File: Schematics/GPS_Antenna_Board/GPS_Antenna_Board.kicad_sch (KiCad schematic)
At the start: 22 parts, among them J1 470804001, U3 SAM-M10Q, U8 LM66100DCKR

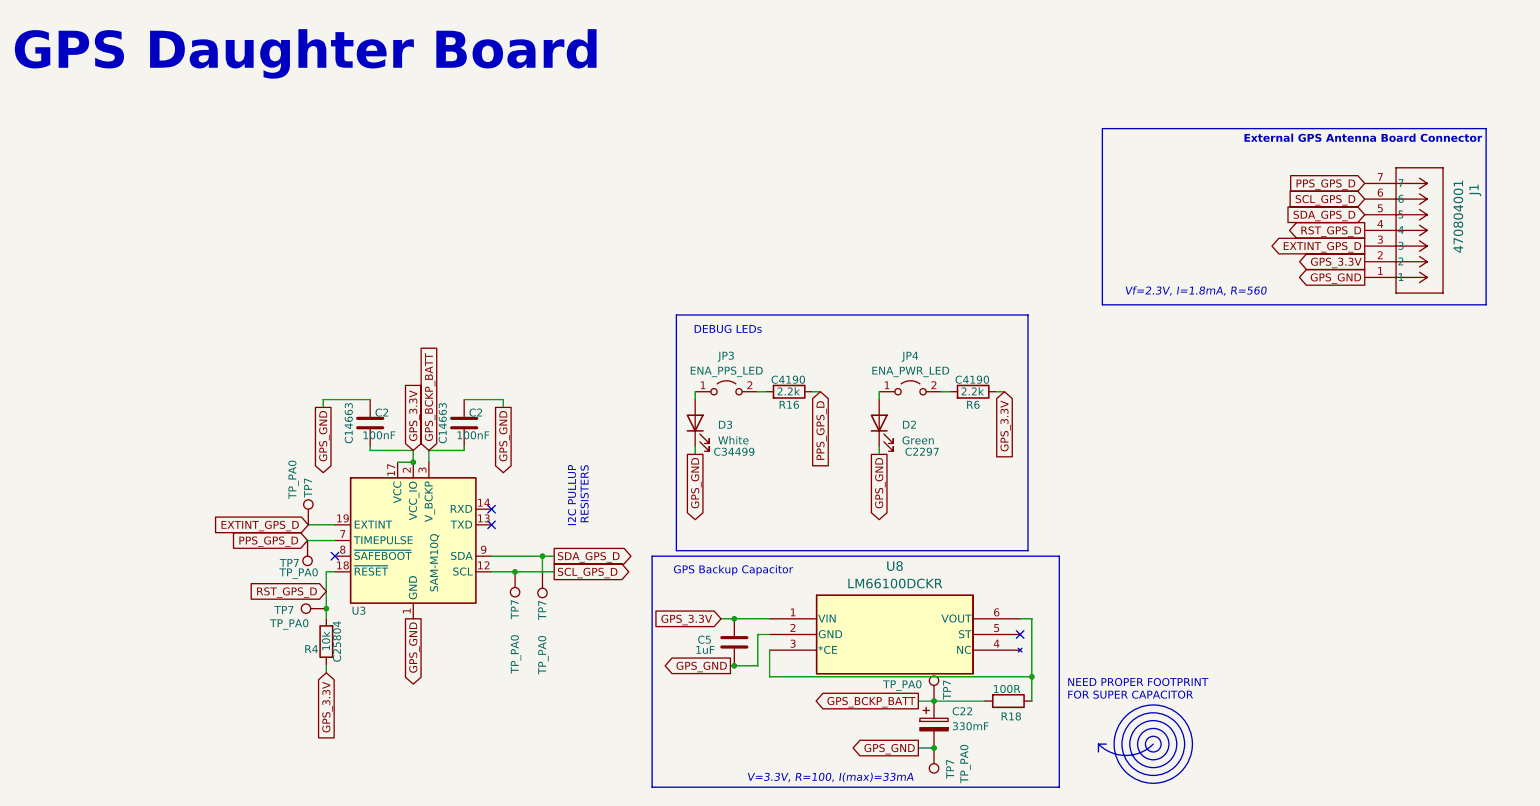
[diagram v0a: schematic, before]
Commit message: Cleaned up GPS antenna schematic
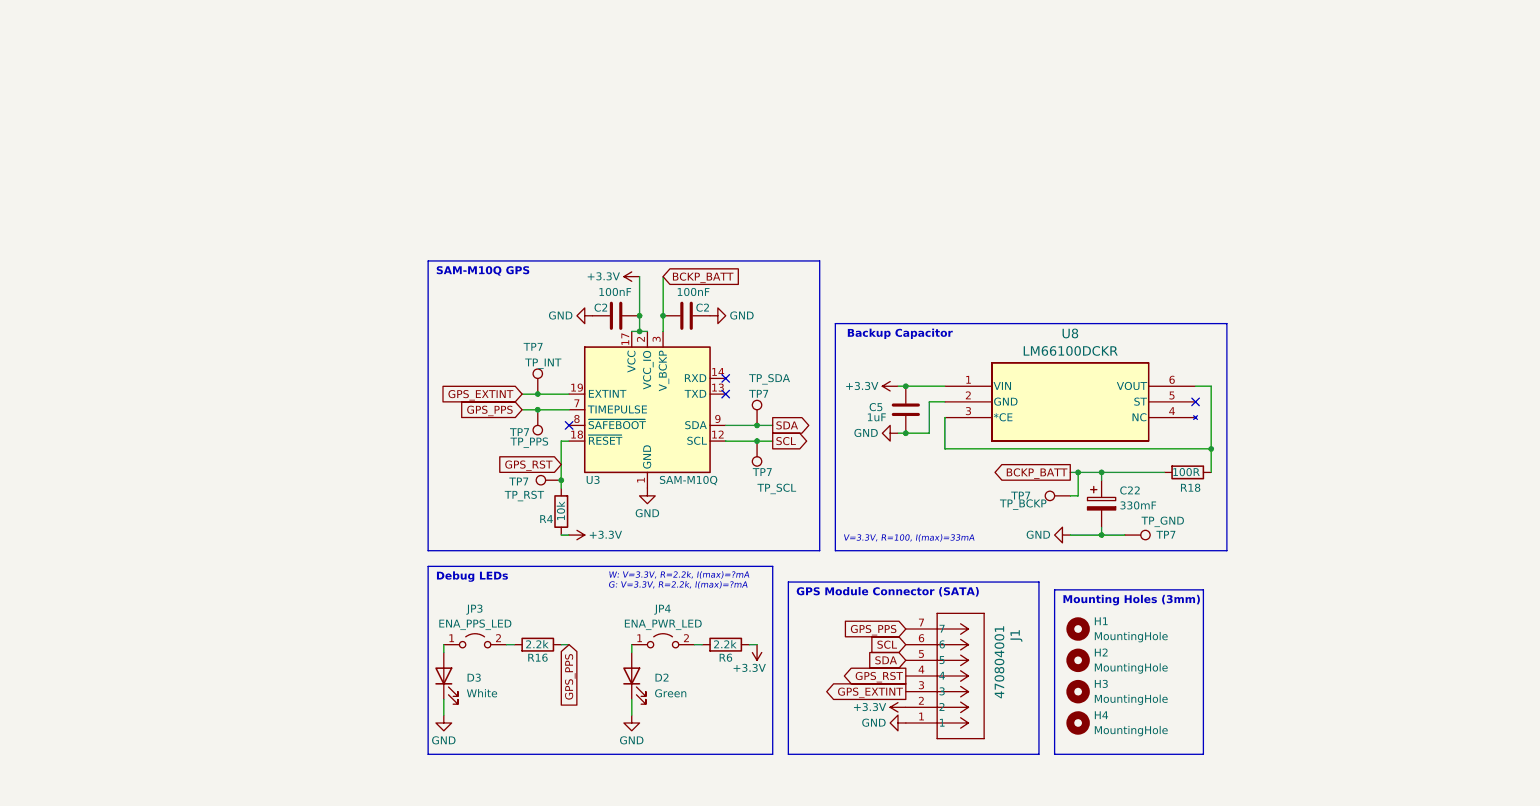
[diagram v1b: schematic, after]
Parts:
- added H1, H2, H3, H4: MountingHole, MountingHole:MountingHole_3mm_Pad, symbol Mechanical:MountingHole
- JP3, JP4: now left out of the parts list
- TP7: value TP_PA0 -> TP_GND; now left out of the parts list
- TP7: value TP_PA0 -> TP_PPS; now left out of the parts list
- TP7: value TP_PA0 -> TP_SDA; now left out of the parts list
- TP7: value TP_PA0 -> TP_BCKP; now left out of the parts list
- TP7: value TP_PA0 -> TP_RST; now left out of the parts list
- TP7: value TP_PA0 -> TP_INT; now left out of the parts list
- TP7: value TP_PA0 -> TP_SCL; now left out of the parts list
- U8: Digikey 296-53541-1-ND -> (none); LCSC (none) -> C2869734
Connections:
- net EXTINT_GPS_D renamed GPS_EXTINT
- net GPS_3.3V renamed +3.3V
- net GPS_BCKP_BATT renamed BCKP_BATT
- net BCKP_BATT: now also C2.1; no longer C2.2
- net GPS_GND renamed GND
- net GND: now also C2.2; no longer C2.1
- net PPS_GPS_D renamed GPS_PPS
- net RST_GPS_D renamed GPS_RST
- net SCL_GPS_D renamed SCL
- net SDA_GPS_D renamed SDA
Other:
- note added: "Backup Capacitor"
- note added: "Debug LEDs"
- note added: "GPS Module Connector (SATA)"
- note added: "Mounting Holes (3mm)"
- note added: "SAM-M10Q GPS"
- note added: "W: V=3.3V, R=2.2k, I(max)=?mA G: V=3.3V, R=2.2k, I(max)=?mA"
- note removed: "DEBUG LEDs"
- note removed: "External GPS Antenna Board Connector"
- note removed: "GPS Backup Capacitor"
- note removed: "GPS Daughter Board"
- note removed: "I2C PULLUP RESISTERS"
- note removed: "NEED PROPER FOOTPRINT FOR SUPER CAPACITOR"
- note removed: "Vf=2.3V, I=1.8mA, R=560"
- company: (none) -> Queen's Rocket Engineering Team
- title: (none) -> QRET 23-24 SRAD GPS Antenna Board
- moved on the sheet: C2, C22, C5, D2, D3, J1, JP3, JP4, R16, R18, R4, R6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

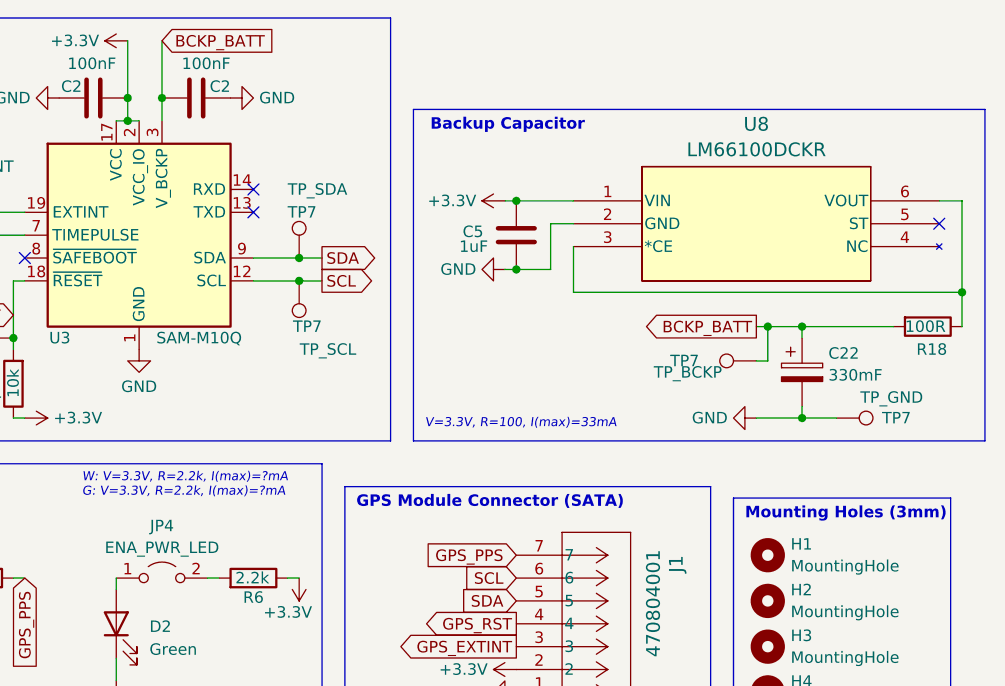
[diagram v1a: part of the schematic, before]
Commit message: Added mounting holes to GPS antenna board
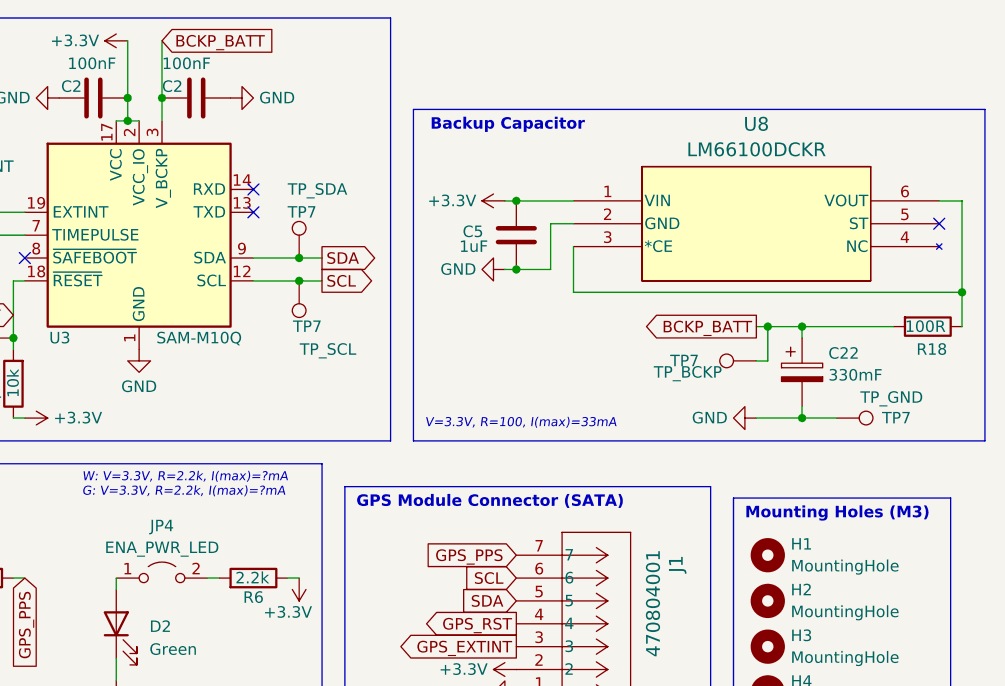
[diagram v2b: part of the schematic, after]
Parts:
- H1, H2, H3, H4: footprint MountingHole:MountingHole_3mm_Pad -> MountingHole:MountingHole_3.2mm_M3_DIN965_Pad
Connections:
- net BCKP_BATT: now also C2.2; no longer C2.1
- net GND: now also C2.1; no longer C2.2
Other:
- note added: "Mounting Holes (M3)"
- note removed: "Mounting Holes (3mm)"
- moved on the sheet: C2
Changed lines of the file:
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@@
     (comment 4 "GRID = 1.27mm")
   )
+  (junction (at 119.38 62.23) (diameter 0) (color 0 0 0 0)
+  )
   (junction (at 99.06 77.47) (diameter 0) (color 0 0 0 0)
   )
@@
   )
   (junction (at 186.69 87.63) (diameter 0) (color 0 0 0 0)
-  )
-  (junction (at 119.38 62.23) (diameter 0) (color 0 0 0 0)
   )
   (junction (at 134.62 80.01) (diameter 0) (color 0 0 0 0)
@@
     (stroke (width 0) (type default))
   )
+  (wire (pts (xy 119.38 55.88) (xy 119.38 62.23))
+    (stroke (width 0) (type default))
+  )
+  (wire (pts (xy 114.3 124.46) (xy 114.3 127))
+    (stroke (width 0) (type default))
+  )
+  (wire (pts (xy 158.75 73.66) (xy 165.1 73.66))
+    (stroke (width 0) (type default))
+  )
+  (wire (pts (xy 162.56 81.28) (xy 162.56 76.2))
+    (stroke (width 0) (type default))
+  )
+  (wire (pts (xy 190.5 97.79) (xy 194.31 97.79))
+    (stroke (width 0) (type default))
+  )
+  (wire (pts (xy 185.42 87.63) (xy 186.69 87.63))
+    (stroke (width 0) (type default))
+  )
+  (wire (pts (xy 93.98 115.57) (xy 95.25 115.57))
+    (stroke (width 0) (type default))
+  )
+  (wire (pts (xy 124.46 115.57) (xy 125.73 115.57))
+    (stroke (width 0) (type default))
+  )
+  (wire (pts (xy 190.5 87.63) (xy 200.66 87.63))
+    (stroke (width 0) (type default))
+  )
+  (wire (pts (xy 186.69 91.44) (xy 186.69 87.63))
+    (stroke (width 0) (type default))
+  )
+  (wire (pts (xy 165.1 78.74) (xy 165.1 83.82))
+    (stroke (width 0) (type default))
+  )
+  (wire (pts (xy 114.3 64.77) (xy 115.57 64.77))
+    (stroke (width 0) (type default))
+  )
+  (wire (pts (xy 134.62 80.01) (xy 137.16 80.01))
+    (stroke (width 0) (type default))
+  )
+  (wire (pts (xy 83.82 115.57) (xy 83.82 116.84))
+    (stroke (width 0) (type default))
+  )
+  (wire (pts (xy 134.62 82.55) (xy 137.16 82.55))
+    (stroke (width 0) (type default))
+  )
+  (wire (pts (xy 102.87 90.17) (xy 102.87 88.9))
+    (stroke (width 0) (type default))
+  )
+  (wire (pts (xy 96.52 77.47) (xy 99.06 77.47))
+    (stroke (width 0) (type default))
+  )
+  (wire (pts (xy 157.48 81.28) (xy 158.75 81.28))
+    (stroke (width 0) (type default))
+  )
+  (wire (pts (xy 83.82 124.46) (xy 83.82 127))
+    (stroke (width 0) (type default))
+  )
+  (wire (pts (xy 114.3 115.57) (xy 114.3 116.84))
+    (stroke (width 0) (type default))
+  )
+  (wire (pts (xy 102.87 82.55) (xy 104.14 82.55))
+    (stroke (width 0) (type default))
+  )
+  (wire (pts (xy 99.06 77.47) (xy 104.14 77.47))
+    (stroke (width 0) (type default))
+  )
+  (wire (pts (xy 185.42 91.44) (xy 186.69 91.44))
+    (stroke (width 0) (type default))
+  )
+  (wire (pts (xy 157.48 73.66) (xy 158.75 73.66))
+    (stroke (width 0) (type default))
+  )
+  (wire (pts (xy 186.69 87.63) (xy 190.5 87.63))
+    (stroke (width 0) (type default))
+  )
+  (wire (pts (xy 129.54 82.55) (xy 134.62 82.55))
+    (stroke (width 0) (type default))
+  )
+  (wire (pts (xy 165.1 83.82) (xy 208.28 83.82))
+    (stroke (width 0) (type default))
+  )
+  (wire (pts (xy 208.28 83.82) (xy 208.28 73.66))
+    (stroke (width 0) (type default))
+  )
+  (wire (pts (xy 190.5 96.52) (xy 190.5 97.79))
+    (stroke (width 0) (type default))
+  )
+  (wire (pts (xy 208.28 73.66) (xy 205.74 73.66))
+    (stroke (width 0) (type default))
+  )
   (wire (pts (xy 119.38 62.23) (xy 119.38 64.77))
-    (stroke (width 0) (type default))
-  )
-  (wire (pts (xy 114.3 124.46) (xy 114.3 127))
-    (stroke (width 0) (type default))
-  )
-  (wire (pts (xy 158.75 73.66) (xy 165.1 73.66))
-    (stroke (width 0) (type default))
-  )
-  (wire (pts (xy 119.38 55.88) (xy 119.38 62.23))
-    (stroke (width 0) (type default))
-  )
-  (wire (pts (xy 162.56 81.28) (xy 162.56 76.2))
-    (stroke (width 0) (type default))
-  )
-  (wire (pts (xy 190.5 97.79) (xy 194.31 97.79))
-    (stroke (width 0) (type default))
-  )
-  (wire (pts (xy 185.42 87.63) (xy 186.69 87.63))
-    (stroke (width 0) (type default))
-  )
-  (wire (pts (xy 93.98 115.57) (xy 95.25 115.57))
-    (stroke (width 0) (type default))
-  )
-  (wire (pts (xy 124.46 115.57) (xy 125.73 115.57))
-    (stroke (width 0) (type default))
-  )
-  (wire (pts (xy 190.5 87.63) (xy 200.66 87.63))
-    (stroke (width 0) (type default))
-  )
-  (wire (pts (xy 186.69 91.44) (xy 186.69 87.63))
-    (stroke (width 0) (type default))
-  )
-  (wire (pts (xy 165.1 78.74) (xy 165.1 83.82))
-    (stroke (width 0) (type default))
-  )
-  (wire (pts (xy 114.3 64.77) (xy 115.57 64.77))
-    (stroke (width 0) (type default))
-  )
-  (wire (pts (xy 134.62 80.01) (xy 137.16 80.01))
-    (stroke (width 0) (type default))
-  )
-  (wire (pts (xy 83.82 115.57) (xy 83.82 116.84))
-    (stroke (width 0) (type default))
-  )
-  (wire (pts (xy 134.62 82.55) (xy 137.16 82.55))
-    (stroke (width 0) (type default))
-  )
-  (wire (pts (xy 102.87 90.17) (xy 102.87 88.9))
-    (stroke (width 0) (type default))
-  )
-  (wire (pts (xy 96.52 77.47) (xy 99.06 77.47))
-    (stroke (width 0) (type default))
-  )
-  (wire (pts (xy 157.48 81.28) (xy 158.75 81.28))
-    (stroke (width 0) (type default))
-  )
-  (wire (pts (xy 83.82 124.46) (xy 83.82 127))
-    (stroke (width 0) (type default))
-  )
-  (wire (pts (xy 114.3 115.57) (xy 114.3 116.84))
-    (stroke (width 0) (type default))
-  )
-  (wire (pts (xy 102.87 82.55) (xy 104.14 82.55))
-    (stroke (width 0) (type default))
-  )
-  (wire (pts (xy 99.06 77.47) (xy 104.14 77.47))
-    (stroke (width 0) (type default))
-  )
-  (wire (pts (xy 185.42 91.44) (xy 186.69 91.44))
-    (stroke (width 0) (type default))
-  )
-  (wire (pts (xy 157.48 73.66) (xy 158.75 73.66))
-    (stroke (width 0) (type default))
-  )
-  (wire (pts (xy 186.69 87.63) (xy 190.5 87.63))
-    (stroke (width 0) (type default))
-  )
-  (wire (pts (xy 129.54 82.55) (xy 134.62 82.55))
-    (stroke (width 0) (type default))
-  )
-  (wire (pts (xy 165.1 83.82) (xy 208.28 83.82))
-    (stroke (width 0) (type default))
-  )
-  (wire (pts (xy 208.28 83.82) (xy 208.28 73.66))
-    (stroke (width 0) (type default))
-  )
-  (wire (pts (xy 190.5 96.52) (xy 190.5 97.79))
-    (stroke (width 0) (type default))
-  )
-  (wire (pts (xy 208.28 73.66) (xy 205.74 73.66))
     (stroke (width 0) (type default))
   )
@@
     (effects (font (size 1 1) italic) (justify left bottom))
   )
-  (text "Mounting Holes (3mm)" (at 184.15 109.22 0)
+  (text "Mounting Holes (M3)" (at 184.15 109.22 0)
     (effects (font (size 1.27 1.27) (thickness 0.254) bold) (justify left bottom))
   )
@@
     )
   )
-  (symbol (lib_id "Device:C") (at 123.19 62.23 90) (unit 1)
+  (symbol (lib_id "Device:C") (at 123.19 62.23 270) (unit 1)
     (in_bom yes) (on_board yes) (dnp no)
-    (property "Reference" "C2" (at 127 60.96 90)
-      (effects (font (size 1.27 1.27)) (justify left))
-    )
-    (property "Value" "100nF" (at 127 58.42 90)
-      (effects (font (size 1.27 1.27)) (justify left))
-    )
-    (property "Footprint" "Capacitor_SMD:C_0603_1608Metric" (at 127 61.2648 0)
+    (property "Reference" "C2" (at 119.38 60.96 90)
+      (effects (font (size 1.27 1.27)) (justify left))
+    )
+    (property "Value" "100nF" (at 119.38 58.42 90)
+      (effects (font (size 1.27 1.27)) (justify left))
+    )
+    (property "Footprint" "Capacitor_SMD:C_0603_1608Metric" (at 119.38 63.1952 0)
       (effects (font (size 1.27 1.27)) hide)
     )
@@
       (effects (font (size 1.27 1.27)) hide)
     )
-    (property "LCSC" "C14663" (at 123.19 65.659 90)
+    (property "LCSC" "C14663" (at 123.19 58.801 90)
       (effects (font (size 1.27 1.27)) hide)
     )
@@
       (effects (font (size 1.27 1.27)) (justify left))
     )
-    (property "Footprint" "MountingHole:MountingHole_3mm_Pad" (at 186.69 128.27 0)
+    (property "Footprint" "MountingHole:MountingHole_3.2mm_M3_DIN965_Pad" (at 186.69 128.27 0)
       (effects (font (size 1.27 1.27)) hide)
     )
@@
       (effects (font (size 1.27 1.27)) (justify left))
     )
-    (property "Footprint" "MountingHole:MountingHole_3mm_Pad" (at 186.69 113.03 0)
+    (property "Footprint" "MountingHole:MountingHole_3.2mm_M3_DIN965_Pad" (at 186.69 113.03 0)
       (effects (font (size 1.27 1.27)) hide)
     )
@@
       (effects (font (size 1.27 1.27)) (justify left))
     )
-    (property "Footprint" "MountingHole:MountingHole_3mm_Pad" (at 186.69 118.11 0)
+    (property "Footprint" "MountingHole:MountingHole_3.2mm_M3_DIN965_Pad" (at 186.69 118.11 0)
       (effects (font (size 1.27 1.27)) hide)
     )
@@
       (effects (font (size 1.27 1.27)) (justify left))
     )
-    (property "Footprint" "MountingHole:MountingHole_3mm_Pad" (at 186.69 123.19 0)
-      (effects (font (size 1.27 1.27)) hide)
-    )
+    (property "Footprint" "MountingHole:MountingHole_3.2mm_M3_DIN965_Pad" (at 186.69 123.19 0)
+      (effects (font (size 1.27 1.27)) hide)
+    )
